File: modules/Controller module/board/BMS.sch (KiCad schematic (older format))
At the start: 20 parts, among them IC1 DW01A, J7 Conn_01x02_Female, Q2 AO3401A, Q3 FS8205A, U3 TP4056

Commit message: Controller module: Schematic and PCB layout
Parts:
- D5: footprint Diode_SMD:D_0805_2012Metric_Pad1.15x1.40mm_HandSolder -> Diode_SMD:D_SMA
- IC1: footprint board:SOT23-6 -> Package_TO_SOT_SMD:SOT-23-6_Handsoldering
- J6: renamed from J7; footprint Connector_PinSocket_2.54mm:PinSocket_1x02_P2.54mm_Vertical -> Board:SolderWire-SMD-BATT
- Q4: renamed from Q3; footprint board:SOP65P640X120-8N -> Board:SOP65P640X120-8N
- U3: footprint board:SOP127P600X175-9N -> Board:SOP127P600X175-9N
- renumbered C5 to C3, C6 to C4, Q2 to Q3, R8 to R16, R9 to R17, R10 to R18, R11 to R19, R12 to R20, R13 to R21
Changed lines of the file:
@@
 $EndDescr
 $Comp
-L Device:R_Small_US R8
+L Device:R_Small_US R16
 U 1 1 619958ED
 P 3250 3550
-F 0 "R8" H 3318 3596 50  0000 L CNN
+F 0 "R16" H 3318 3596 50  0000 L CNN
 F 1 "1k" H 3318 3505 50  0000 L CNN
 F 2 "Resistor_SMD:R_0805_2012Metric_Pad1.20x1.40mm_HandSolder" H 3250 3550 50  0001 C CNN
@@
 	3250 3650 3250 3750
 $Comp
-L Device:R_Small_US R10
+L Device:R_Small_US R18
 U 1 1 619979BF
 P 3950 3550
-F 0 "R10" H 4018 3596 50  0000 L CNN
+F 0 "R18" H 4018 3596 50  0000 L CNN
 F 1 "1k" H 4018 3505 50  0000 L CNN
 F 2 "Resistor_SMD:R_0805_2012Metric_Pad1.20x1.40mm_HandSolder" H 3950 3550 50  0001 C CNN
@@
 	5550 3800 5550 3950
 $Comp
-L power:GND #PWR032
+L power:GND #PWR033
 U 1 1 6199BAE9
 P 5400 3650
-F 0 "#PWR032" H 5400 3400 50  0001 C CNN
+F 0 "#PWR033" H 5400 3400 50  0001 C CNN
 F 1 "GND" H 5405 3477 50  0000 C CNN
 F 2 "" H 5400 3650 50  0001 C CNN
@@
 F 0 "U3" H 6250 4367 50  0000 C CNN
 F 1 "TP4056" H 6250 4276 50  0000 C CNN
-F 2 "board:SOP127P600X175-9N" H 6250 3700 50  0001 L BNN
+F 2 "Board:SOP127P600X175-9N" H 6250 3700 50  0001 L BNN
 F 3 "" H 6250 3700 50  0001 L BNN
 F 4 "1.75mm" H 6250 3700 50  0001 L BNN "MAXIMUM_PACKAGE_HEIGHT"
@@
 	5400 3500 5650 3500
 $Comp
-L power:GND #PWR034
+L power:GND #PWR035
 U 1 1 6199F212
 P 5550 4250
-F 0 "#PWR034" H 5550 4000 50  0001 C CNN
+F 0 "#PWR035" H 5550 4000 50  0001 C CNN
 F 1 "GND" H 5555 4077 50  0000 C CNN
 F 2 "" H 5550 4250 50  0001 C CNN
@@
 $EndComp
 $Comp
-L Device:R_Small_US R12
+L Device:R_Small_US R20
 U 1 1 6199F776
 P 5550 4050
-F 0 "R12" H 5618 4096 50  0000 L CNN
+F 0 "R20" H 5618 4096 50  0000 L CNN
 F 1 "1.2k" H 5618 4005 50  0000 L CNN
 F 2 "Resistor_SMD:R_0805_2012Metric_Pad1.20x1.40mm_HandSolder" H 5550 4050 50  0001 C CNN
@@
 Connection ~ 6950 4100
 $Comp
-L power:GND #PWR035
+L power:GND #PWR036
 U 1 1 619A0A50
 P 6950 4200
-F 0 "#PWR035" H 6950 3950 50  0001 C CNN
+F 0 "#PWR036" H 6950 3950 50  0001 C CNN
 F 1 "GND" H 6955 4027 50  0000 C CNN
 F 2 "" H 6950 4200 50  0001 C CNN
@@
 	7500 1450 7500 1550
 $Comp
-L power:GND #PWR037
+L power:GND #PWR038
 U 1 1 619B7FBD
 P 7500 1550
-F 0 "#PWR037" H 7500 1300 50  0001 C CNN
+F 0 "#PWR038" H 7500 1300 50  0001 C CNN
 F 1 "GND" H 7505 1377 50  0000 C CNN
 F 2 "" H 7500 1550 50  0001 C CNN
@@
 	7750 3450 8050 3450
 $Comp
-L Device:CP_Small C6
+L Device:CP_Small C4
 U 1 1 619B9D05
 P 8050 3650
-F 0 "C6" H 7800 3700 50  0000 L CNN
+F 0 "C4" H 7800 3700 50  0000 L CNN
 F 1 "10uF" H 7800 3600 50  0000 L CNN
 F 2 "Capacitor_SMD:C_0805_2012Metric_Pad1.18x1.45mm_HandSolder" H 8050 3650 50  0001 C CNN
@@
 	8050 3550 8050 3450
 $Comp
-L Transistor_FET:AO3401A Q2
+L Transistor_FET:AO3401A Q3
 U 1 1 61A47D24
 P 3750 1850
-F 0 "Q2" V 4092 1850 50  0000 C CNN
+F 0 "Q3" V 4092 1850 50  0000 C CNN
 F 1 "AO3401A" V 4001 1850 50  0000 C CNN
 F 2 "Package_TO_SOT_SMD:SOT-23" H 3950 1775 50  0001 L CIN
@@
 F 0 "D5" H 4100 2100 50  0000 R CNN
 F 1 "D_Schottky" H 4250 2200 50  0000 R CNN
-F 2 "Diode_SMD:D_0805_2012Metric_Pad1.15x1.40mm_HandSolder" H 4100 1950 50  0001 C CNN
+F 2 "Diode_SMD:D_SMA" H 4100 1950 50  0001 C CNN
 F 3 "~" H 4100 1950 50  0001 C CNN
 	1    4100 1950
@@
 $EndComp
 $Comp
-L Device:R_Small_US R9
+L Device:R_Small_US R17
 U 1 1 61A4EED8
 P 3750 2350
-F 0 "R9" H 3818 2396 50  0000 L CNN
+F 0 "R17" H 3818 2396 50  0000 L CNN
 F 1 "10k" H 3818 2305 50  0000 L CNN
 F 2 "Resistor_SMD:R_0805_2012Metric_Pad1.20x1.40mm_HandSolder" H 3750 2350 50  0001 C CNN
@@
 $EndComp
 $Comp
-L power:GND #PWR029
+L power:GND #PWR030
 U 1 1 61A4FE63
 P 3750 2500
-F 0 "#PWR029" H 3750 2250 50  0001 C CNN
+F 0 "#PWR030" H 3750 2250 50  0001 C CNN
 F 1 "GND" H 3755 2327 50  0000 C CNN
 F 2 "" H 3750 2500 50  0001 C CNN
@@
 	3250 2150 3750 2150
 $Comp
-L power:+5V #PWR027
+L power:+5V #PWR028
 U 1 1 61A68B7A
 P 3250 2050
-F 0 "#PWR027" H 3250 1900 50  0001 C CNN
+F 0 "#PWR028" H 3250 1900 50  0001 C CNN
 F 1 "+5V" H 3265 2223 50  0000 C CNN
 F 2 "" H 3250 2050 50  0001 C CNN
@@
 	3250 2050 3250 2150
 $Comp
-L power:VCC #PWR031
+L power:VCC #PWR032
 U 1 1 61A6A8F1
 P 4100 1650
-F 0 "#PWR031" H 4100 1500 50  0001 C CNN
+F 0 "#PWR032" H 4100 1500 50  0001 C CNN
 F 1 "VCC" H 4115 1823 50  0000 C CNN
 F 2 "" H 4100 1650 50  0001 C CNN
@@
 F 0 "IC1" H 6150 2517 50  0000 C CNN
 F 1 "DW01A" H 6150 2426 50  0000 C CNN
-F 2 "board:SOT23-6" H 6150 1950 50  0001 L BNN
+F 2 "Package_TO_SOT_SMD:SOT-23-6_Handsoldering" H 6150 1950 50  0001 L BNN
 F 3 "" H 6150 1950 50  0001 L BNN
 F 4 "DW01A" H 6150 1950 50  0001 L BNN "MPN"
@@
 $EndComp
 $Comp
-L FS8205A:FS8205A Q3
+L FS8205A:FS8205A Q4
 U 1 1 61A73178
 P 7200 1950
-F 0 "Q3" H 7444 1996 50  0000 L CNN
+F 0 "Q4" H 7444 1996 50  0000 L CNN
 F 1 "FS8205A" H 7444 1905 50  0000 L CNN
-F 2 "board:SOP65P640X120-8N" H 7200 1950 50  0001 L BNN
+F 2 "Board:SOP65P640X120-8N" H 7200 1950 50  0001 L BNN
 F 3 "" H 7200 1950 50  0001 L BNN
 F 4 "Fortune Semiconductor" H 7200 1950 50  0001 L BNN "MANUFACTURER"
@@
 	8050 3750 8050 3900
 $Comp
-L Connector:Conn_01x02_Female J7
+L Connector:Conn_01x02_Female J6
 U 1 1 619B0A12
 P 8500 3700
-F 0 "J7" H 8528 3676 50  0000 L CNN
+F 0 "J6" H 8528 3676 50  0000 L CNN
 F 1 "Conn_01x02_Female" H 8528 3585 50  0000 L CNN
-F 2 "Connector_PinSocket_2.54mm:PinSocket_1x02_P2.54mm_Vertical" H 8500 3700 50  0001 C CNN
+F 2 "Board:SolderWire-SMD-BATT" H 8500 3700 50  0001 C CNN
 F 3 "~" H 8500 3700 50  0001 C CNN
 	1    8500 3700
@@
 	7300 2500 7650 2500
 $Comp
-L Device:R_Small_US R11
+L Device:R_Small_US R19
 U 1 1 61A90319
 P 5550 1450
-F 0 "R11" H 5350 1500 50  0000 L CNN
+F 0 "R19" H 5350 1500 50  0000 L CNN
 F 1 "100R" H 5300 1400 50  0000 L CNN
 F 2 "Resistor_SMD:R_0805_2012Metric_Pad1.20x1.40mm_HandSolder" H 5550 1450 50  0001 C CNN
@@
 $EndComp
 $Comp
-L Device:CP_Small C5
+L Device:CP_Small C3
 U 1 1 61A910D8
 P 5550 1850
-F 0 "C5" H 5300 1900 50  0000 L CNN
+F 0 "C3" H 5300 1900 50  0000 L CNN
 F 1 "0.1uF" H 5300 1800 50  0000 L CNN
 F 2 "Capacitor_SMD:C_0805_2012Metric_Pad1.18x1.45mm_HandSolder" H 5550 1850 50  0001 C CNN
@@
 	5550 1250 5550 1350
 $Comp
-L Device:R_Small_US R13
+L Device:R_Small_US R21
 U 1 1 61A9D27D
 P 6950 1450
-F 0 "R13" V 6750 1400 50  0000 L CNN
+F 0 "R21" V 6750 1400 50  0000 L CNN
 F 1 "1k" V 6850 1400 50  0000 L CNN
 F 2 "Resistor_SMD:R_0805_2012Metric_Pad1.20x1.40mm_HandSolder" H 6950 1450 50  0001 C CNN
@@
 Connection ~ 7200 2500
 $Comp
-L power:+5V #PWR0101
+L power:+5V #PWR039
 U 1 1 61B31398
 P 8250 1800
-F 0 "#PWR0101" H 8250 1650 50  0001 C CNN
+F 0 "#PWR039" H 8250 1650 50  0001 C CNN
 F 1 "+5V" H 8265 1973 50  0000 C CNN
 F 2 "" H 8250 1800 50  0001 C CNN
@@
 $EndComp
 $Comp
-L power:GND #PWR049
+L power:GND #PWR040
 U 1 1 61B2C876
 P 8450 2300
-F 0 "#PWR049" H 8450 2050 50  0001 C CNN
+F 0 "#PWR040" H 8450 2050 50  0001 C CNN
 F 1 "GND" H 8455 2127 50  0000 C CNN
 F 2 "" H 8450 2300 50  0001 C CNN
@@
 $EndComp
 $Comp
-L power:+5V #PWR048
+L power:+5V #PWR034
 U 1 1 61B44133
 P 5550 3400
-F 0 "#PWR048" H 5550 3250 50  0001 C CNN
+F 0 "#PWR034" H 5550 3250 50  0001 C CNN
 F 1 "+5V" H 5565 3573 50  0000 C CNN
 F 2 "" H 5550 3400 50  0001 C CNN
@@
 $EndComp
 $Comp
-L power:+5V #PWR050
+L power:+5V #PWR037
 U 1 1 61B44D3F
 P 7000 3200
-F 0 "#PWR050" H 7000 3050 50  0001 C CNN
+F 0 "#PWR037" H 7000 3050 50  0001 C CNN
 F 1 "+5V" H 7015 3373 50  0000 C CNN
 F 2 "" H 7000 3200 50  0001 C CNN
@@
 $EndComp
 $Comp
-L power:+5V #PWR033
+L power:+5V #PWR029
 U 1 1 61B45860
 P 3250 3350
-F 0 "#PWR033" H 3250 3200 50  0001 C CNN
+F 0 "#PWR029" H 3250 3200 50  0001 C CNN
 F 1 "+5V" H 3265 3523 50  0000 C CNN
 F 2 "" H 3250 3350 50  0001 C CNN
@@
 $EndComp
 $Comp
-L power:+5V #PWR036
+L power:+5V #PWR031
 U 1 1 61B45E6A
 P 3950 3350
-F 0 "#PWR036" H 3950 3200 50  0001 C CNN
+F 0 "#PWR031" H 3950 3200 50  0001 C CNN
 F 1 "+5V" H 3965 3523 50  0000 C CNN
 F 2 "" H 3950 3350 50  0001 C CNN

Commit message: Controller module: PCB complete
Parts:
- removed TP1, TP2, TP3, TP4: TestPoint, TestPoint:TestPoint_Pad_1.5x1.5mm, symbol Connector:TestPoint
- J6: footprint Board:SolderWire-SMD-BATT -> Board:SolderWire_1x02_P2.00mm
- renumbered D3 to D4, D4 to D5, D5 to D6, R16 to R17, R17 to R18, R18 to R19, R19 to R20, R20 to R21, R21 to R22
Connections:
- wire segments 79 -> 81
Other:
- moved on the sheet: C3, C4, D4, D5, D6, IC1, J6, Q3, Q4, R17, R18, R19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

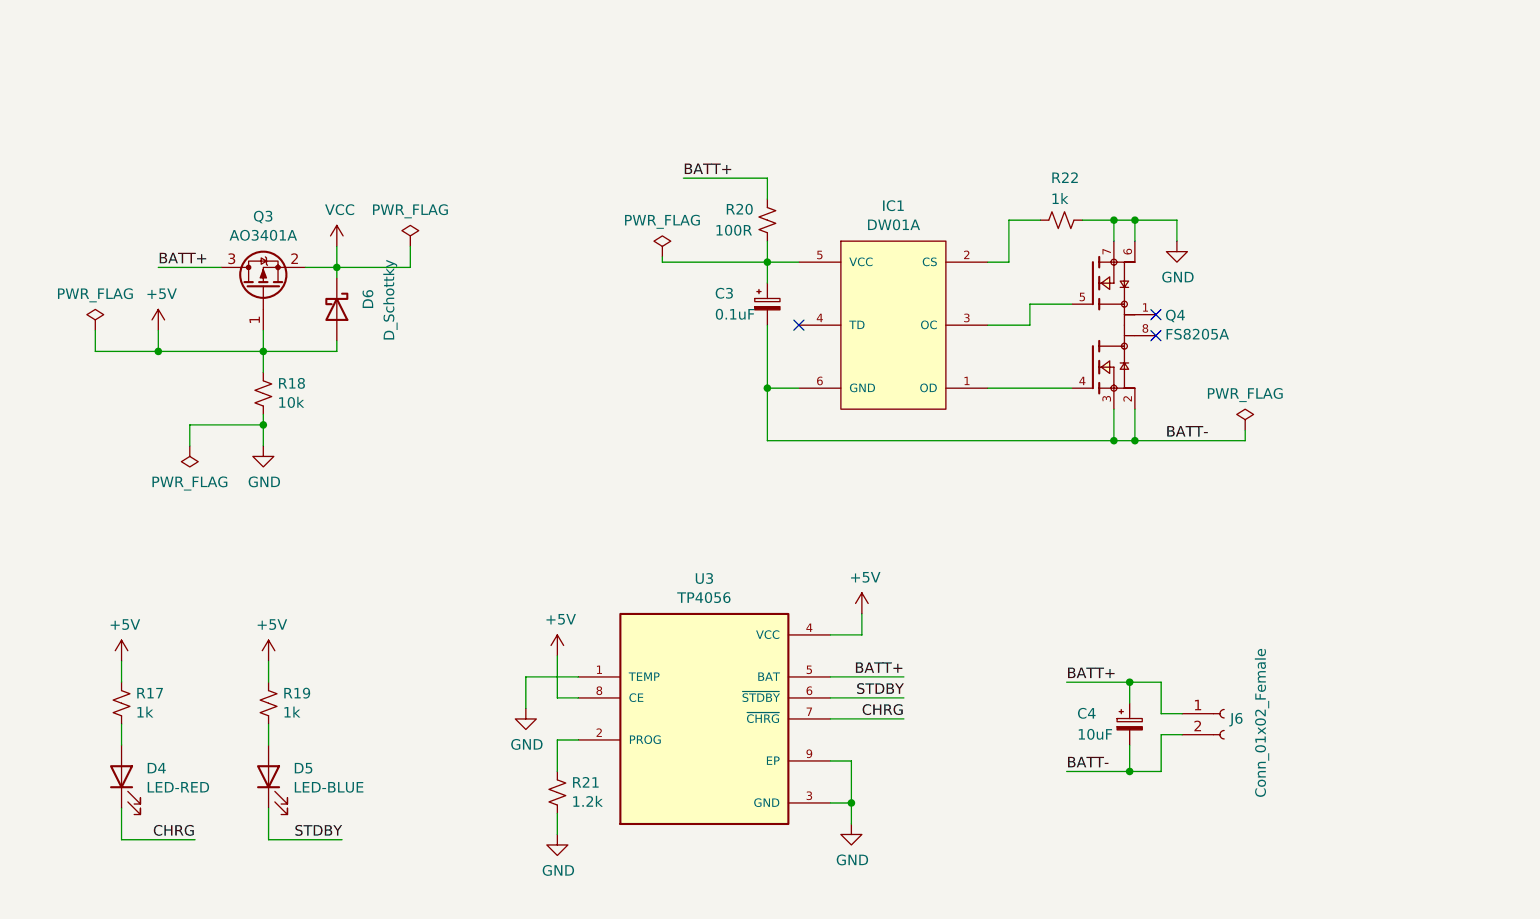
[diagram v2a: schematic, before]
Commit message: Controller module: PCB modular
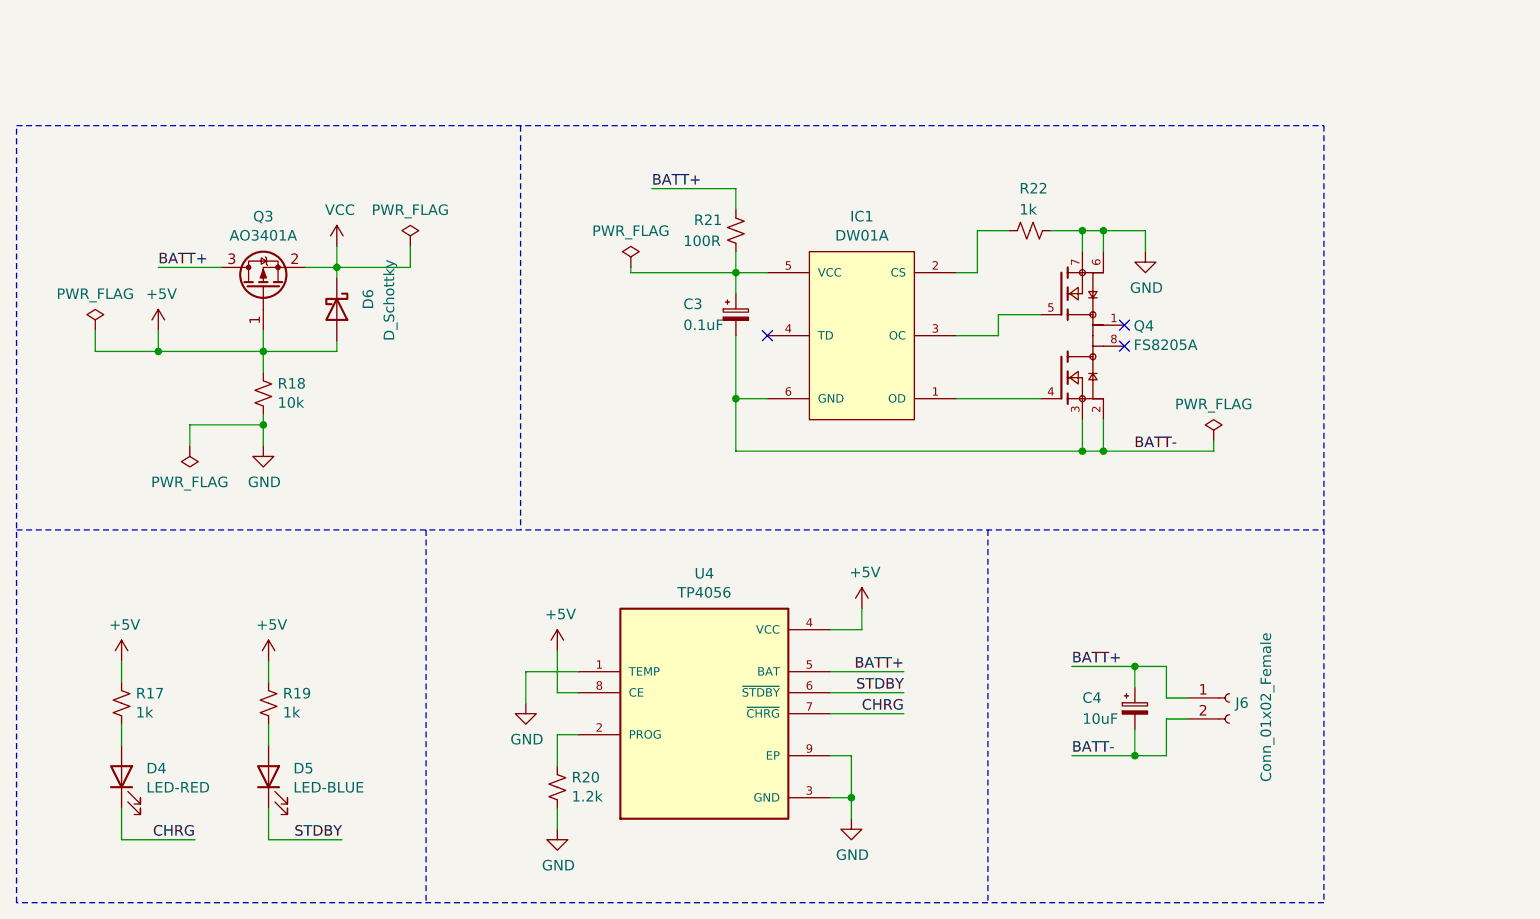
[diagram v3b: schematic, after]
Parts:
- renumbered R21 to R20, R20 to R21, U3 to U4
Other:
- moved on the sheet: C3, C4, IC1, J6, Q4, R20, R21, R22, U4
